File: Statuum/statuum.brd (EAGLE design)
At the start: 99.1 x 80 mm, 73 parts, among them IC1 LM317MABT, J1 POWER_JACKPTH, J2 NRJ3HF-1, J3 RCJ-21XXMILL, Q1 2N5484, Q10 ZVN4306A, Q11 ZVN4306A, Q12 ZVN4306A, Q2 2N5484, Q3 ZVN4306A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

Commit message: Desktop version changed to IRF510 output
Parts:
- removed Q10, Q11, Q12, Q9: ZVN4306A, my-tran:TO-92
- removed R28: 2.61k, my-res:AXIAL-0.4
- removed R29: 240, my-res:AXIAL-0.4
- C10: value 470u -> 100uF
- C11: value 4700u -> 10uF; device SparkFun-Capacitors:CPOL-RADIAL-1000UF-63V -> my-cap:CPOL-RADIAL-10UF-25V-SM
- C12: value 4700u -> 0.1uF; device SparkFun-Capacitors:CPOL-RADIAL-1000UF-63V -> SparkFun-Capacitors:CAP-PTH-SMALL
- C13: value 10uF -> 0.47uF; device my-cap:CPOL-RADIAL-10UF-25V-SM -> capacitor-wima:C5B3.5
- C14: value 0.1uF -> 10uF; device SparkFun-Capacitors:CAP-PTH-SMALL -> my-cap:CPOL-RADIAL-10UF-25V-SM
- C15: value 100uF -> 470u
- C16: value 0.1uF -> 470u; device SparkFun-Capacitors:CAP-PTH-SMALL -> my-cap:CPOL-RADIAL-8/3.5
- C3: value 10uF -> 4700u; device my-cap:CPOL-RADIAL-10UF-25V-SM -> SparkFun-Capacitors:CPOL-RADIAL-1000UF-63V
- C4: value 470u -> 10uF; device my-cap:CPOL-RADIAL-8/3.5 -> my-cap:CPOL-RADIAL-10UF-25V-SM
- C6: value 10uF -> 470u; device my-cap:CPOL-RADIAL-10UF-25V-SM -> my-cap:CPOL-RADIAL-8/3.5
- C7: value 0.47uF -> 4700u; device capacitor-wima:C5B3.5 -> SparkFun-Capacitors:CPOL-RADIAL-1000UF-63V
- C9: value 470u -> 0.1uF; device my-cap:CPOL-RADIAL-8/3.5 -> SparkFun-Capacitors:CAP-PTH-SMALL
- D10, D9: value (none) -> BLUE; device SparkFun-DiscreteSemi:DIODE-1N4001 -> my:LED3MM-SM
- D3, D4: value BLUE -> (none); device my:LED3MM-SM -> SparkFun-DiscreteSemi:DIODE-1N4001
- Q3, Q4: value ZVN4306A -> IRF510; device my-tran:TO-92 -> my-tran:TO220-HORIZ
- Q5, Q6: value ZVN4306A -> 2N5484
- Q7, Q8: value 2N5484 -> IRF510; device my-tran:TO-92 -> my-tran:TO220-HORIZ
- R10: value TD90 -> 5.6; device my:PTD902 -> my-res:AXIAL-0.4
- R11: value 6.8 -> 4.3
- R12, R25: value 6.2 -> 4.3
- R13: value 100 -> 240
- R14: value 100 -> 2.61k
- R18, R19, R4, R5: value 4.7k -> 820
- R24: value 6.8 -> 5.6
- R26: value 100 -> 4.3
- R27: value 100 -> TD90; device my-res:AXIAL-0.4 -> my:PTD902
- moved LOGO1 76.5 mm to (12.7, 72.4), turned to 180 degrees
- moved R14 74.9 mm to (85.1, 39.4), turned to 0 degrees
- moved C8 61.4 mm to (95.2, 39.4), turned to 180 degrees
- moved R13 61.3 mm to (85.1, 35.6), turned to 180 degrees
- moved C14 59.8 mm to (35.6, 22.9), turned to 90 degrees
- moved C15 56.1 mm to (41.9, 34.9), turned to 270 degrees
- moved C3 55.3 mm to (74.9, 49.5), turned to 0 degrees
- moved C13 55.0 mm to (40.6, 45.7), turned to 0 degrees
- moved C9 51.0 mm to (94.0, 35.6), turned to 0 degrees
- moved C7 50.9 mm to (91.4, 49.5), turned to 180 degrees
- moved Q6 49.7 mm to (54.6, 58.4), turned to 270 degrees
- moved Q7 42.2 mm to (43.2, 16.5), turned to 180 degrees
- moved Q8 42.0 mm to (57.1, 16.5), turned to 180 degrees
- moved C16 40.9 mm to (53.3, 34.9)
- moved D7 39.2 mm to (71.1, 35.6), turned to 180 degrees
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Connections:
- removed net N$26: Q11.2, R26.P$1
- removed net N$27: Q12.2, R27.P$1
- net GND: now also C10.2, C4.2, C7.2, C9.2, D10.K, D3.A, D4.A, R14.P$1, R26.P$1, R27.R1.1, R27.R2.1; no longer C13.2, C15.2, C16.2, C6.2, D4.K, D5.A, D7.A, R10.R1.1, R10.R2.1, R25.P$1, R28.P$1
- net IN_L: now also R27.R1.2; no longer R10.R1.2
- net IN_L*: now also R27.R1.3; no longer R10.R1.3
- net IN_R: now also R27.R2.2; no longer R10.R2.2
- net IN_R*: now also R27.R2.3; no longer R10.R2.3
- net N$1: no longer R13.P$2
- net N$10: now also Q4.3; no longer Q4.1, Q6.1
- net N$11: now also Q3.2, R10.P$1; no longer Q3.3, Q5.3, R11.P$1
- net N$12: now also C6.1, Q4.2, R11.P$1; no longer C4.1, Q3.1, Q4.3, Q5.1, Q6.3
- net N$13: now also D3.C, D5.A; no longer D5.C, D6.A
- net N$15: no longer R14.P$2
- net N$16: now also Q5.2; no longer Q7.2, R26.P$2
- net N$17: now also Q5.3, Q6.1; no longer Q7.3, Q8.1
- net N$18: now also Q6.2; no longer Q8.2
- net N$19: now also Q6.3; no longer Q8.3
- net N$20: now also Q7.1; no longer Q9.2
- net N$21: now also Q8.1; no longer Q10.2
- net N$22: now also Q8.3, R26.P$2; no longer Q10.1, Q12.1, R25.P$2
- net N$23: now also C13.1, Q7.2; no longer C7.1, Q11.3, Q9.3
- net N$24: now also D9.A; no longer D3.A
- net N$25: now also D10.A, D9.K; no longer D3.K, D4.A
- net N$28: now also C13.2; no longer C7.2, R27.P$2
- net N$29: now also C15.1, C16.1, Q8.2, R25.P$1; no longer C10.1, C9.1, Q10.3, Q11.1, Q12.3, Q9.1
- net N$30: now also D4.C, D6.A; no longer D7.C, D8.A
- net N$32: now also C8.1, C9.1, D8.A, R13.P$1, R14.P$2; no longer C13.1, C14.1, D10.A, R28.P$2, R29.P$1
- net N$33: now also C3.1, C7.1, D5.C, D7.C; no longer C11.1, C12.1, D8.C, D9.C
- net N$5: now also Q3.1; no longer Q3.2
- net N$7: now also Q3.3, R11.P$2; no longer Q5.2, R13.P$1
- net N$8: now also Q4.1; no longer Q4.2
- net N$9: now also Q7.3, R25.P$2; no longer Q6.2, R14.P$1
- net OUT_L: now also C6.2; no longer C4.2
- net OUT_R: now also C15.2, C16.2; no longer C10.2, C9.2
- net VCC: now also C10.1, C11.1, C12.1, C14.1, C4.1, D7.A, D8.C, Q5.1, R10.P$2, R13.P$2; no longer C15.1, C16.1, C3.1, C6.1, C8.1, D10.C, D9.A, Q7.1, R11.P$2, R29.P$2
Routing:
- net N$29: track 52.3 -> 24.0 mm, vias 1 -> 0
- net N$12: track 44.9 -> 24.0 mm, vias 1 -> 0
- net N$5: track 4.97 -> 21.2 mm
- net N$20: track 4.97 -> 19.0 mm
- net VCC: track 252.0 -> 239.7 mm, vias 2 -> 1
- net N$15: track 21.9 -> 10.2 mm
- net N$28: track 21.9 -> 10.2 mm
- net N$8: track 9.83 -> 21.2 mm
- net N$21: track 9.83 -> 21.2 mm
- net N$1: track 37.1 -> 26.2 mm
- net N$16: track 37.1 -> 26.2 mm
- net N$26: track 10.4 -> 0.00 mm
- net N$10: track 15.3 -> 5.08 mm
- net N$33: track 76.3 -> 86.4 mm
- net N$32: track 33.1 -> 42.7 mm
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
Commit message: Mounting holes
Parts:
- added H1: MOUNT-PAD-ROUND3.2, holes:3,2-PAD
- added H2: MOUNT-HOLE3.2, holes:3,2
- moved LOGO1 42.5 mm to (55.2, 72.4)
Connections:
- net GND: now also H1.B3,2
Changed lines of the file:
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@@
 <wire x1="99.695" y1="80.01" x2="99.695" y2="0" width="0.254" layer="20"/>
 <wire x1="99.695" y1="0" x2="0.635" y2="0" width="0.254" layer="20"/>
-<hole x="4.445" y="76.2" drill="3.2"/>
-<hole x="95.885" y="76.2" drill="3.2"/>
 <wire x1="82.55" y1="11.43" x2="82.55" y2="26.67" width="0.6096" layer="41"/>
 <wire x1="82.55" y1="26.67" x2="76.2" y2="33.02" width="0.6096" layer="41" curve="90"/>
@@
 <attribute name="VALUE" x="85.979" y="26.924" size="0.8128" layer="27" ratio="20" rot="R90"/>
 </element>
-<element name="LOGO1" library="my" package="LOGO-MANTIS" value="LOGO-MANTIS" x="12.7" y="72.39" smashed="yes" rot="R180"/>
+<element name="LOGO1" library="my" package="LOGO-MANTIS" value="LOGO-MANTIS" x="55.245" y="72.39" smashed="yes" rot="R180"/>
 <element name="Q3" library="my-tran" package="TO220-HORIZ" value="IRF510" x="21.59" y="16.51" smashed="yes" rot="R180">
 <attribute name="NAME" x="25.4" y="11.303" size="0.8128" layer="25" ratio="20" rot="R180"/>
@@
 <attribute name="VALUE" x="49.911" y="28.321" size="0.8128" layer="27" font="vector" ratio="20" rot="R180"/>
 </element>
+<element name="H1" library="holes" package="3,2-PAD" value="MOUNT-PAD-ROUND3.2" x="5.715" y="74.93"/>
+<element name="H2" library="holes" package="3,2" value="MOUNT-HOLE3.2" x="94.615" y="71.12"/>
 </elements>
 <signals>
@@
 <via x="3.175" y="64.77" extent="1-16" drill="0.6"/>
 <via x="3.175" y="69.85" extent="1-16" drill="0.6"/>
-<via x="7.62" y="77.47" extent="1-16" drill="0.6"/>
 <via x="12.7" y="77.47" extent="1-16" drill="0.6"/>
 <via x="17.78" y="77.47" extent="1-16" drill="0.6"/>
 <via x="48.26" y="77.47" extent="1-16" drill="0.6"/>
-<via x="53.34" y="77.47" extent="1-16" drill="0.6"/>
+<via x="57.15" y="77.47" extent="1-16" drill="0.6"/>
 <via x="72.39" y="77.47" extent="1-16" drill="0.6"/>
 <via x="77.47" y="77.47" extent="1-16" drill="0.6"/>
 <via x="82.55" y="77.47" extent="1-16" drill="0.6"/>
-<via x="97.155" y="72.39" extent="1-16" drill="0.6"/>
-<via x="97.155" y="67.31" extent="1-16" drill="0.6"/>
+<via x="97.155" y="77.47" extent="1-16" drill="0.6"/>
+<via x="97.155" y="66.04" extent="1-16" drill="0.6"/>
 <via x="97.155" y="62.23" extent="1-16" drill="0.6"/>
 <via x="97.155" y="57.15" extent="1-16" drill="0.6"/>
@@
 <via x="60.96" y="43.815" extent="1-16" drill="0.6"/>
 <via x="60.96" y="55.88" extent="1-16" drill="0.6"/>
-<via x="58.42" y="73.66" extent="1-16" drill="0.6"/>
+<via x="58.42" y="71.12" extent="1-16" drill="0.6"/>
 <via x="62.23" y="66.04" extent="1-16" drill="0.6"/>
 <via x="64.77" y="71.12" extent="1-16" drill="0.6"/>
@@
 <via x="17.145" y="39.37" extent="1-16" drill="0.6"/>
 <via x="48.895" y="38.735" extent="1-16" drill="0.6"/>
+<contactref element="H1" pad="B3,2"/>
 </signal>
 <signal name="N$6">

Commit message: Mounting holes
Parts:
- moved H1 0.90 mm to (5.08, 75.6)
- moved H2 0.64 mm to (95.2, 71.1)
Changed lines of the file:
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@@
 <attribute name="VALUE" x="49.911" y="28.321" size="0.8128" layer="27" font="vector" ratio="20" rot="R180"/>
 </element>
-<element name="H1" library="holes" package="3,2-PAD" value="MOUNT-PAD-ROUND3.2" x="5.715" y="74.93"/>
-<element name="H2" library="holes" package="3,2" value="MOUNT-HOLE3.2" x="94.615" y="71.12"/>
+<element name="H1" library="holes" package="3,2-PAD" value="MOUNT-PAD-ROUND3.2" x="5.08" y="75.565"/>
+<element name="H2" library="holes" package="3,2" value="MOUNT-HOLE3.2" x="95.25" y="71.12"/>
 </elements>
 <signals>

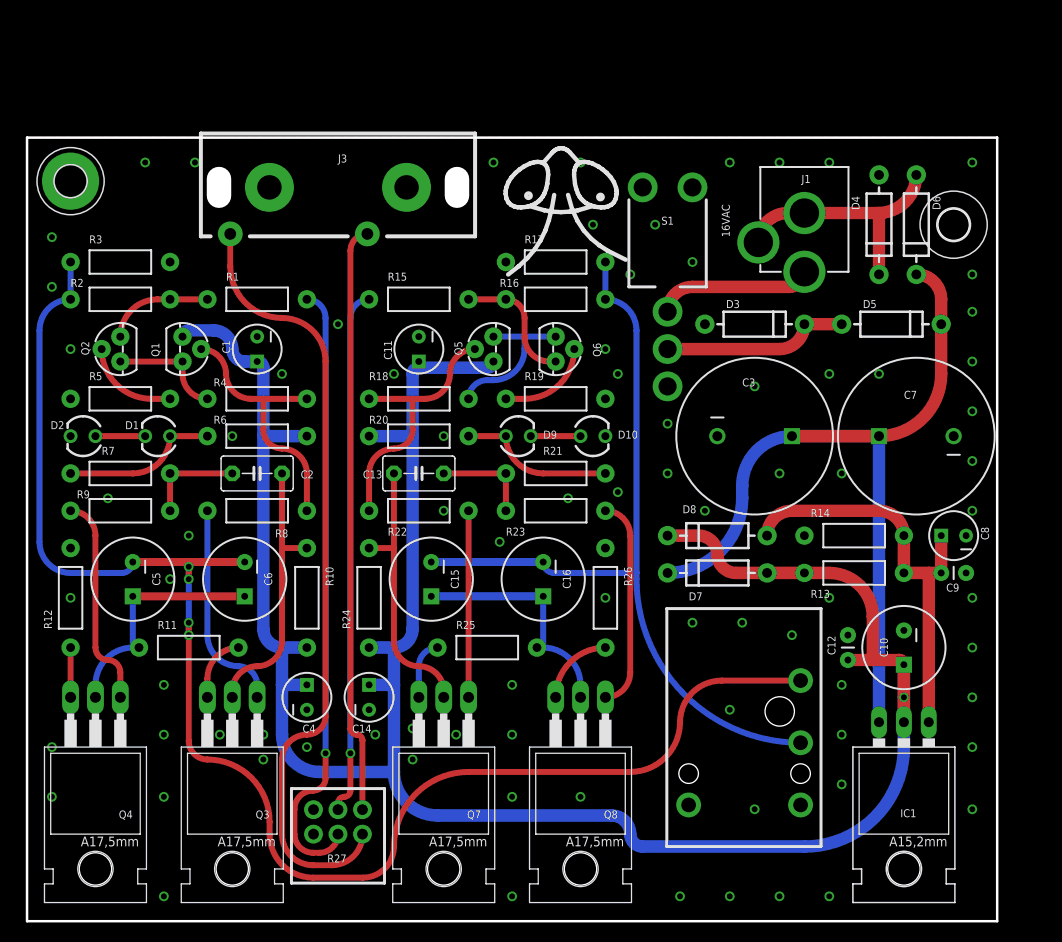
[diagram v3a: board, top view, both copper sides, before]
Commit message: VBE multiplier added
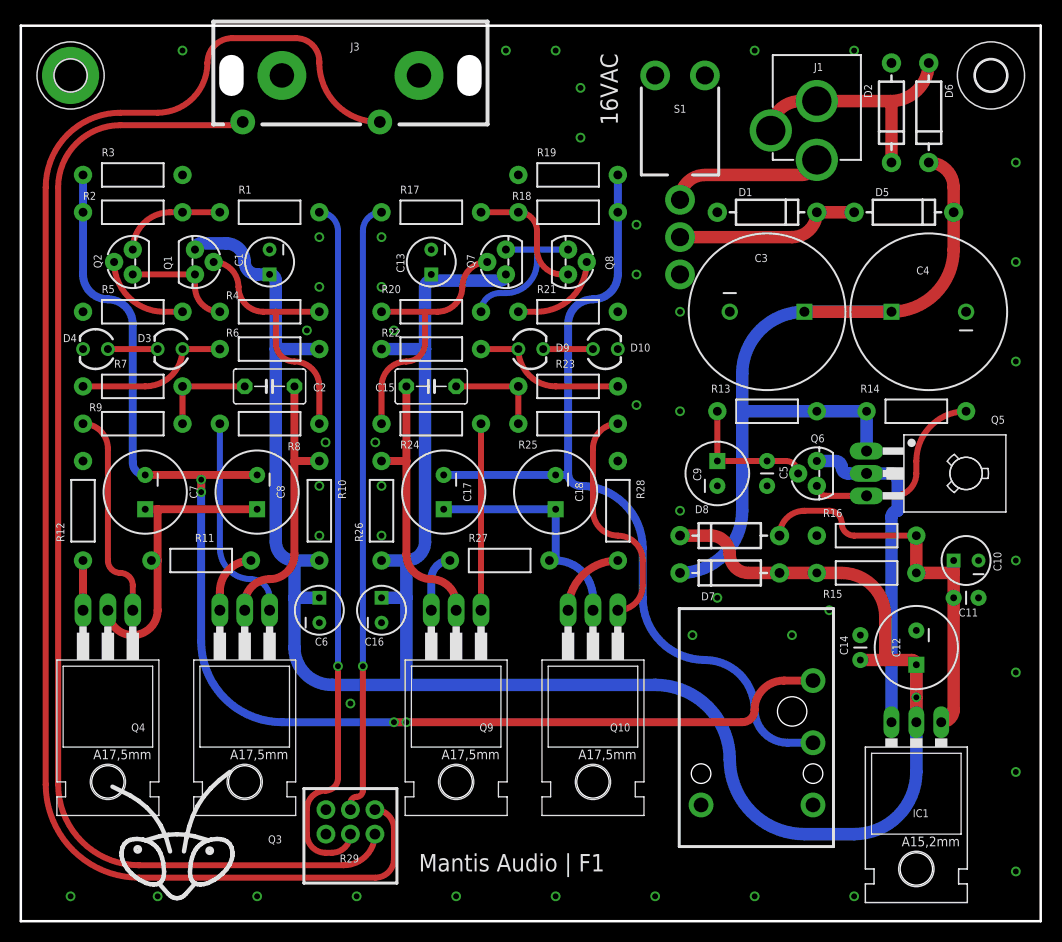
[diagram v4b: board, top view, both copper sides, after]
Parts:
- added C17, C18: 470u, my-cap:CPOL-RADIAL-8/3.5
- added Q10, Q9: IRF510, my-tran:TO220-HORIZ
- added R28: 4.3, my-res:AXIAL-0.4
- added R29: TD90, my:PTD902
- C1: device my-cap:CPOL-RADIAL-10UF-25V-SM -> my-cap:CPOL-RADIAL-5/2.5-SM
- C10: value 100uF -> 10uF; device my-cap:CPOL-RADIAL-8/3.5 -> my-cap:CPOL-RADIAL-5/2.5-SM
- C11, C14: value 10uF -> 0.1uF; device my-cap:CPOL-RADIAL-10UF-25V-SM -> SparkFun-Capacitors:CAP-PTH-SMALL
- C12: value 0.1uF -> 100uF/35V; device SparkFun-Capacitors:CAP-PTH-SMALL -> my-cap:CPOL-RADIAL-8/3.5
- C13: value 0.47uF -> 10uF; device capacitor-wima:C5B3.5 -> my-cap:CPOL-RADIAL-5/2.5-SM
- C15: value 470u -> 0.47uF; device my-cap:CPOL-RADIAL-8/3.5 -> capacitor-wima:C5B3.5
- C16, C6: value 470u -> 10uF; device my-cap:CPOL-RADIAL-8/3.5 -> my-cap:CPOL-RADIAL-5/2.5-SM
- C3: value 4700u -> 4700uF/35V
- C4: value 10uF -> 4700uF/35V; device my-cap:CPOL-RADIAL-10UF-25V-SM -> my-cap:CPOL-RADIAL-16/7.5
- C5: value 470u -> 1uF; device my-cap:CPOL-RADIAL-8/3.5 -> SparkFun-Capacitors:CAP-PTH-SMALL
- C7: value 4700u -> 470u; device SparkFun-Capacitors:CPOL-RADIAL-1000UF-63V -> my-cap:CPOL-RADIAL-8/3.5
- C8: value 10uF -> 470u; device my-cap:CPOL-RADIAL-10UF-25V-SM -> my-cap:CPOL-RADIAL-8/3.5
- C9: value 0.1uF -> 47uF/35V; device SparkFun-Capacitors:CAP-PTH-SMALL -> my-cap:CPOL-RADIAL-6.5/2.5
- D1, D2: value BLUE -> (none); device my:LED3MM-SM -> SparkFun-DiscreteSemi:DIODE-1N4001
- D3, D4: value (none) -> BLUE; device SparkFun-DiscreteSemi:DIODE-1N4001 -> my:LED3MM-SM
- Q5: value 2N5484 -> BD140; device my-tran:TO-92 -> transistor-pnp:TO126
- Q6: value 2N5484 -> BC547
- Q7, Q8: value IRF510 -> 2N5484; device my-tran:TO220-HORIZ -> my-tran:TO-92
- R13: value 240 -> 10k
- R14: value 2.61k -> 220
- R15: value 680 -> 240
- R16: value 3.3k -> 2.61k
- R17: value 100k -> 680
- R18: value 820 -> 3.3k
- R19: value 820 -> 100k
- R20: value 4.7k -> 820
- R21: value 1Meg -> 820
- R22: value 100 -> 4.7k
- R23: value 100 -> 1Meg
- R24: value 5.6 -> 100
- R25: value 4.3 -> 100
- R26: value 4.3 -> 5.6
- R27: value TD90 -> 4.3; device my:PTD902 -> my-res:AXIAL-0.4
- moved D2 88.9 mm to (88.9, 82.5), turned to 270 degrees
- moved D4 81.0 mm to (7.62, 58.4), turned to 180 degrees
- moved C7 78.9 mm to (12.7, 43.8), turned to 270 degrees
- moved LOGO1 74.7 mm to (15.9, 8.89), turned to 0 degrees
- moved C4 74.7 mm to (92.7, 62.2), turned to 180 degrees
- moved C8 71.3 mm to (24.1, 43.8), turned to 270 degrees
- moved D1 66.3 mm to (76.2, 72.4), turned to 0 degrees
- moved C5 65.9 mm to (76.2, 47.0)
- moved C11 60.2 mm to (95.2, 33.0), turned to 0 degrees
- moved D3 59.7 mm to (15.2, 58.4), turned to 180 degrees
- moved R15 53.6 mm to (86.4, 35.6)
- moved Q7 51.2 mm to (49.5, 67.3), turned to 90 degrees
- moved Q8 50.8 mm to (55.9, 67.3), turned to 270 degrees
- moved C14 50.3 mm to (85.7, 26.7)
- moved Q5 45.0 mm to (91.4, 45.7), turned to 270 degrees
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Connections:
- removed net N$33: C3.1, C7.1, D5.C, D6.C, D7.C, IC1.3
- new net N$26: Q5.3, Q6.1, R14.P$2
- new net N$27: C5.1, C9.1, Q6.2, R13.P$1
- new net N$34: C3.1, C4.1, D5.C, D6.C, D7.C, Q5.1, R13.P$2, R14.P$1
- new net N$36: IC1.3, Q5.2, Q6.3
- net GND: now also C13.2, C16.2, C5.2, C6.2, D1.A, D2.A, D4.K, R16.P$1, R21.P$1, R28.P$1, R29.R1.1, R29.R2.1; no longer C7.2, C8.2, D2.K, D3.A, D4.A, R14.P$1, R17.P$1, R26.P$1, R27.R1.1, R27.R2.1
- net IN_L: now also R29.R1.2; no longer R27.R1.2
- net IN_L*: now also R29.R1.3; no longer R27.R1.3
- net IN_R: now also R17.P$2, R29.R2.2; no longer R15.P$2, R27.R2.2
- net IN_R*: now also R29.R2.3; no longer R27.R2.3
- net N$12: now also C7.1, C8.1; no longer C5.1, C6.1
- net N$13: now also D1.C; no longer D3.C
- net N$14: now also D3.A; no longer D1.A
- net N$16: now also Q7.2, R20.P$2, R24.P$2; no longer Q5.2, R18.P$2, R22.P$2
- net N$17: now also Q7.3, Q8.1, R20.P$1; no longer Q5.3, Q6.1, R18.P$1
- net N$18: now also Q8.2, R21.P$2; no longer Q6.2, R19.P$2
- net N$19: now also Q8.3, R17.P$1, R18.P$2; no longer Q6.3, R15.P$1, R16.P$2
- net N$20: now also Q9.1, R24.P$1; no longer Q7.1, R22.P$1
- net N$21: now also Q10.1, R25.P$1; no longer Q8.1, R23.P$1
- net N$22: now also Q10.3, R28.P$2; no longer Q8.3, R26.P$2
- net N$23: now also C15.1, Q9.2, R26.P$1; no longer C13.1, Q7.2, R24.P$1
- net N$24: now also R22.P$1, R23.P$2; no longer R20.P$1, R21.P$2
- net N$28: now also C15.2, R23.P$1, R25.P$2; no longer C13.2, R21.P$1, R23.P$2
- net N$29: now also C17.1, C18.1, Q10.2, R27.P$1; no longer C15.1, C16.1, Q8.2, R25.P$1
- net N$30: now also D2.C; no longer D4.C
- net N$32: now also C10.1, C11.1, R15.P$1, R16.P$2; no longer C8.1, C9.1, R13.P$1, R14.P$2
- net N$4: now also D3.K, D4.A; no longer D1.K, D2.A
- net N$9: now also Q9.3, R27.P$2; no longer Q7.3, R25.P$2
- net OUT_L: now also C7.2, C8.2; no longer C5.2, C6.2
- net OUT_R: now also C17.2, C18.2, R18.P$1, R19.P$2; no longer C15.2, C16.2, R16.P$1, R17.P$2
- net VCC: now also C13.1, C16.1, C6.1, Q7.1, R15.P$2, R22.P$2, R26.P$2; no longer C10.1, C11.1, C4.1, Q5.1, R13.P$2, R20.P$2, R24.P$2
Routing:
- net IN_R*: track 60.0 -> 151.2 mm
- net N$33: track 86.4 -> 0.00 mm
- net N$34: track 0.00 -> 85.4 mm
- net IN_L*: track 78.0 -> 119.7 mm
- net N$36: track 0.00 -> 34.1 mm
- net N$26: track 0.00 -> 20.0 mm
- net OUT_L: track 150.8 -> 131.9 mm
- net N$27: track 0.00 -> 13.9 mm
- net IN_L: track 62.7 -> 71.6 mm
- net IN_R: track 53.4 -> 62.3 mm
- net OUT_R: track 78.8 -> 84.8 mm
- net N$12: track 24.0 -> 29.6 mm
- net VCC: track 239.7 -> 243.8 mm
- net N$21: track 21.2 -> 23.3 mm
- net N$32: track 42.7 -> 40.7 mm
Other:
- board size 99.1 x 80 mm -> 104.1 x 91.4 mm
- board text added: "Mantis Audio | F1"
